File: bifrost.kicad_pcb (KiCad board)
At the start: 2 copper layers, 74 parts, among them J1 395430602, J10 Conn_0.1_01x04, J11 Conn_0.1_01x04, J12 Conn_0.1_01x06, J2 393800102, J3 393800102, J4 393800103, J5 393800103, J6 393800103, J7 393800103, J8 SJ_3524, J9 Conn_0.1_01x03, Q1 2N7002, SW1 SW_Push, SW2 SW_Push, SW3 SW_Push, SW4 SW_Push

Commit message: Begin placement
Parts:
- removed the C10 at (65.9, 49.0)
- removed the C12 at (89.1, 60.7)
- removed the C7 at (101.0, 19.0)
- removed the C8 at (50.8, 64.0)
- removed the C9 at (85.9, 34.0)
- removed the D5 at (68.1, 68.5)
- removed D6: BLU, LED_SMD:LED_1206_3216Metric_Pad1.42x1.75mm_HandSolder
- removed the J11 at (22.7, 62.8)
- removed the J3 at (51.6, 48.8)
- removed JP5, JP6: SolderJumper_2_Open, Jumper:SolderJumper-2_P1.3mm_Open_Pad1.0x1.5mm
- removed Q1: 2N7002, Package_TO_SOT_SMD:SOT-23
- removed the R13 at (113.1, 30.4)
- removed the R16 at (101.3, 38.2)
- removed the R17 at (78.2, 70.8)
- removed the R24 at (113.1, 33.4)
- removed the R25 at (83.0, 67.9)
- added C2: 0.1uF, Capacitor_SMD:C_0805_2012Metric_Pad1.15x1.40mm_HandSolder, F.Cu at (152.4, 35.6)
- added C3: 0.1uF, Capacitor_SMD:C_0805_2012Metric_Pad1.15x1.40mm_HandSolder, F.Cu at (137.9, 35.7)
- added C4: 0.1uF, Capacitor_SMD:C_0805_2012Metric_Pad1.15x1.40mm_HandSolder, F.Cu at (165.9, 21.2)
- added C5: 1uF, Capacitor_SMD:C_0805_2012Metric_Pad1.15x1.40mm_HandSolder, F.Cu at (158.2, 30.9)
- added C6: 0.1uF, Capacitor_SMD:C_0805_2012Metric_Pad1.15x1.40mm_HandSolder, F.Cu at (165.9, 24.1)
- added D1: RED, LED_SMD:LED_1206_3216Metric_Pad1.42x1.75mm_HandSolder, F.Cu at (132.5, 35.9)
- added J10: Conn_0.1_01x04, Connector_PinHeader_2.54mm:PinHeader_1x04_P2.54mm_Vertical, F.Cu at (22.7, 62.8)
- added J12: Micro_SD_Card_Det_Single, bifrost:microSD_Molex_1051620001, B.Cu at (179.6, 100.6)
- added R1: 1K, Resistor_SMD:R_0805_2012Metric_Pad1.15x1.40mm_HandSolder, F.Cu at (158.2, 33.9)
- added R14: 1K, Resistor_SMD:R_0805_2012Metric_Pad1.15x1.40mm_HandSolder, F.Cu at (163.0, 33.9)
- added R4: 2K, Resistor_SMD:R_0805_2012Metric_Pad1.15x1.40mm_HandSolder, F.Cu at (163.0, 30.9)
- added U1: 74LVC1G17, Package_TO_SOT_SMD:SOT-23-5_HandSoldering, F.Cu at (152.9, 31.8)
- added U2: 74LVC1G14, Package_TO_SOT_SMD:SOT-23-5_HandSoldering, F.Cu at (166.5, 17.4)
- added U3: 74AHCT125, Package_SO:SOIC-14_3.9x8.7mm_P1.27mm, F.Cu at (188.0, 104.1)
- D2: renamed from D4; value RED -> GRN
- D3: renamed from D2; value AMB -> BLU
- D4: renamed from D3; value AMB -> BLU
- D5: renamed from D1; value AMB -> BLU
- J1: value 395430602 -> 395430002
- J2: value 393800102 -> 395430002; footprint bifrost:TerminalBlock_Molex_393800102_1x02_P6.35mm_Horizontal -> bifrost:TerminalBlock_Molex_395430602_1x02_P5.00mm_Horizontal
- J3: renamed from J4; value 393800103 -> 393570003; footprint bifrost:TerminalBlock_Molex_393800103_1x03_P6.35mm_Horizontal -> bifrost:TerminalBlock_Molex_393570003_1x03_P3.50mm_Horizontal
- J4: renamed from J5; value 393800103 -> 393570003; footprint bifrost:TerminalBlock_Molex_393800103_1x03_P6.35mm_Horizontal -> bifrost:TerminalBlock_Molex_393570003_1x03_P3.50mm_Horizontal
- J5: renamed from J6; value 393800103 -> 393570003; footprint bifrost:TerminalBlock_Molex_393800103_1x03_P6.35mm_Horizontal -> bifrost:TerminalBlock_Molex_393570003_1x03_P3.50mm_Horizontal
- J6: renamed from J7; value 393800103 -> 393570003; footprint bifrost:TerminalBlock_Molex_393800103_1x03_P6.35mm_Horizontal -> bifrost:TerminalBlock_Molex_393570003_1x03_P3.50mm_Horizontal
- JP1, JP2: value Jumper_NC_Small -> Jumper_NO_Small
- JP3: value Jumper_NC_Dual -> Jumper_NO_Small; footprint Connector_PinHeader_2.54mm:PinHeader_1x03_P2.54mm_Vertical -> Connector_PinHeader_2.54mm:PinHeader_1x02_P2.54mm_Vertical
- JP4: value SolderJumper_2_Open -> Jumper_NO_Small; footprint Jumper:SolderJumper-2_P1.3mm_Open_Pad1.0x1.5mm -> Connector_PinHeader_2.54mm:PinHeader_1x02_P2.54mm_Vertical
- R15: renamed from R23; value 470 -> 330
- R16: renamed from R18; value 470 -> 330
- R17: renamed from R19; value 470 -> 330
- R18: renamed from R20; value 470 -> 330
- R9: value 100 -> 10K
- moved A1 215.6 mm to (218.4, 96.5), turned to 270 degrees
- moved H3 172.4 mm to (231.1, 134.6)
- moved J7 160.0 mm to (185.4, 121.9), turned to 90 degrees
- moved H2 141.5 mm to (231.0, 88.9)
- moved H4 129.0 mm to (185.4, 134.6)
- moved JP3 123.9 mm to (156.6, 24.6)
- moved H1 115.1 mm to (185.4, 88.9)
- moved R9 100.5 mm to (165.9, 27.1)
- moved J1 97.3 mm to (121.9, 40.6)
- moved JP1 84.0 mm to (161.2, 24.6)
- moved J2 60.6 mm to (142.2, 43.2)
- moved JP4 53.5 mm to (161.2, 17.4)
- moved JP2 45.5 mm to (156.6, 17.4)
- renumbered C11 to C1, C5 to C10, C4 to C11, C6 to C12, C1 to C7, C2 to C8, C3 to C9, J12 to J11, J8 to J7, J9 to J8, J10 to J9, R3 to R10, R4 to R12, R12 to R13, R5 to R19, R26 to R2, R14 to R20, R1 to R21, R7 to R22, R6 to R23, R15 to R24, R2 to R25, R8 to R26, R27 to R3, R28 to R5, R29 to R6, R21 to R7, R22 to R8, SW3 to SW2, SW2 to SW3
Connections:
- A1 pad 12: /LED1 -> /BTN4
- A1 pad 13: /LED2 -> /~CS
- A1 pad 14: /LED3 -> /MOSI
- A1 pad 15: /BTN4 -> /MISO
- A1 pad 16: Net-(A1-Pad16) -> /SCK
- A1 pad 22: Net-(A1-Pad22) -> /LED1
- A1 pad 25: Net-(A1-Pad25) -> /LED2
- A1 pad 26: Net-(A1-Pad26) -> /LED3
- A1 pad 27: Net-(A1-Pad27) -> /A5V
- A1 pad 29: Net-(A1-Pad29) -> GND
- D2 pad 1: GND -> Net-(D2-Pad1)
- D2 pad 2: Net-(D4-Pad2) -> +5V
- D3 pad 1: GND -> Net-(D3-Pad1)
- D3 pad 2: Net-(D2-Pad2) -> /LED1
- D4 pad 1: GND -> Net-(D4-Pad1)
- D4 pad 2: Net-(D3-Pad2) -> /LED2
- D5 pad 1: GND -> Net-(D5-Pad1)
- D5 pad 2: Net-(D1-Pad2) -> /LED3
- J2 pad 1: VCC -> +5V
- J3 pad 1: VCC -> +5V
- J4 pad 1: VCC -> +5V
- J5 pad 1: VDD -> +5V
- J6 pad 1: VDD -> +5V
- JP1 pad 1: +5V -> /A5V
- JP1 pad 2: Net-(A1-Pad27) -> +5V
- JP2 pad 1: Net-(A1-Pad29) -> Net-(JP2-Pad1)
- JP2 pad 2: GND -> Net-(A1-Pad2)
- JP3 pad 1: VCC -> Net-(A1-Pad28)
- JP3 pad 2: +5V -> /BT_RST
- JP4 pad 1: /BT_TX -> Net-(JP4-Pad1)
- JP4 pad 2: Net-(A1-Pad2) -> Net-(A1-Pad1)
- R15 pad 1: +5V -> Net-(D2-Pad1)
- R15 pad 2: Net-(D4-Pad2) -> GND
- R16 pad 1: /LED1 -> Net-(D3-Pad1)
- R16 pad 2: Net-(D1-Pad2) -> GND
- R17 pad 1: /LED2 -> Net-(D4-Pad1)
- R17 pad 2: Net-(D2-Pad2) -> GND
- R18 pad 1: /LED3 -> Net-(D5-Pad1)
- R18 pad 2: Net-(D3-Pad2) -> GND
- R9 pad 1: Net-(Q1-Pad1) -> /BT_ST
- R9 pad 2: /BT_ST -> GND

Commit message: Do most placement
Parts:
- removed the JP3 at (156.6, 24.6)
- removed the R2 at (103.3, 44.1)
- added JP2: Jumper_NO_Small, Connector_PinHeader_2.54mm:PinHeader_1x02_P2.54mm_Vertical, F.Cu at (162.6, 80.0)
- added R4: 330, Resistor_SMD:R_0805_2012Metric_Pad1.15x1.40mm_HandSolder, B.Cu at (170.2, 62.2)
- A1: footprint bifrost:Arduino_Nano -> Module:Arduino_Nano
- C1, C10, C11, C12, C2, C3, C4, C5, C6, C7, C8, C9, R1, R10, R11, R12, R13, R14, R15, R16, R17, R18, R19, R20, R21, R22, R23, R24, R25, R26, R3, R5, R6, R7, R8, R9: moved to B.Cu
- J11: footprint Connector_PinSocket_2.54mm:PinSocket_1x08_P2.54mm_Vertical -> Connector_PinSocket_2.54mm:PinSocket_1x06_P2.54mm_Vertical
- R2: renamed from R4; moved to B.Cu
- moved J9 182.6 mm to (199.1, 86.4)
- moved J10 180.1 mm to (199.1, 99.1)
- moved J11 174.1 mm to (199.1, 80.0), turned to 180 degrees
- moved J3 147.7 mm to (186.7, 56.9), turned to 180 degrees
- moved C12 138.5 mm to (187.3, 106.7), turned to 90 degrees
- moved C9 136.9 mm to (179.1, 113.0), turned to 90 degrees
- moved R25 126.4 mm to (185.4, 119.4), turned to 90 degrees
- moved SW1 122.1 mm to (172.4, 110.6), turned to 45 degrees
- moved SW3 121.3 mm to (179.3, 117.4), turned to 45 degrees
- moved SW4 121.2 mm to (186.0, 110.6), turned to 45 degrees
- moved J4 115.1 mm to (174.0, 56.9), turned to 180 degrees
- moved R26 115.0 mm to (190.5, 109.9), turned to 90 degrees
- moved D5 111.8 mm to (162.6, 111.8), turned to 90 degrees
- moved SW2 110.9 mm to (179.2, 103.8), turned to 45 degrees
- moved R22 110.5 mm to (181.0, 100.3), turned to 90 degrees
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- renumbered JP2 to JP3
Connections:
- J1 pad 1: VBUS -> GND
- J1 pad 2: GND -> VBUS
- R3 pad 1: Net-(A1-Pad9) -> Net-(A1-Pad8)
- R3 pad 2: /OUT2 -> /OUT1
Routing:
- added copper zone on B.Cu, net GND
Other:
- board outline added: 73.7 x 71.1 mm

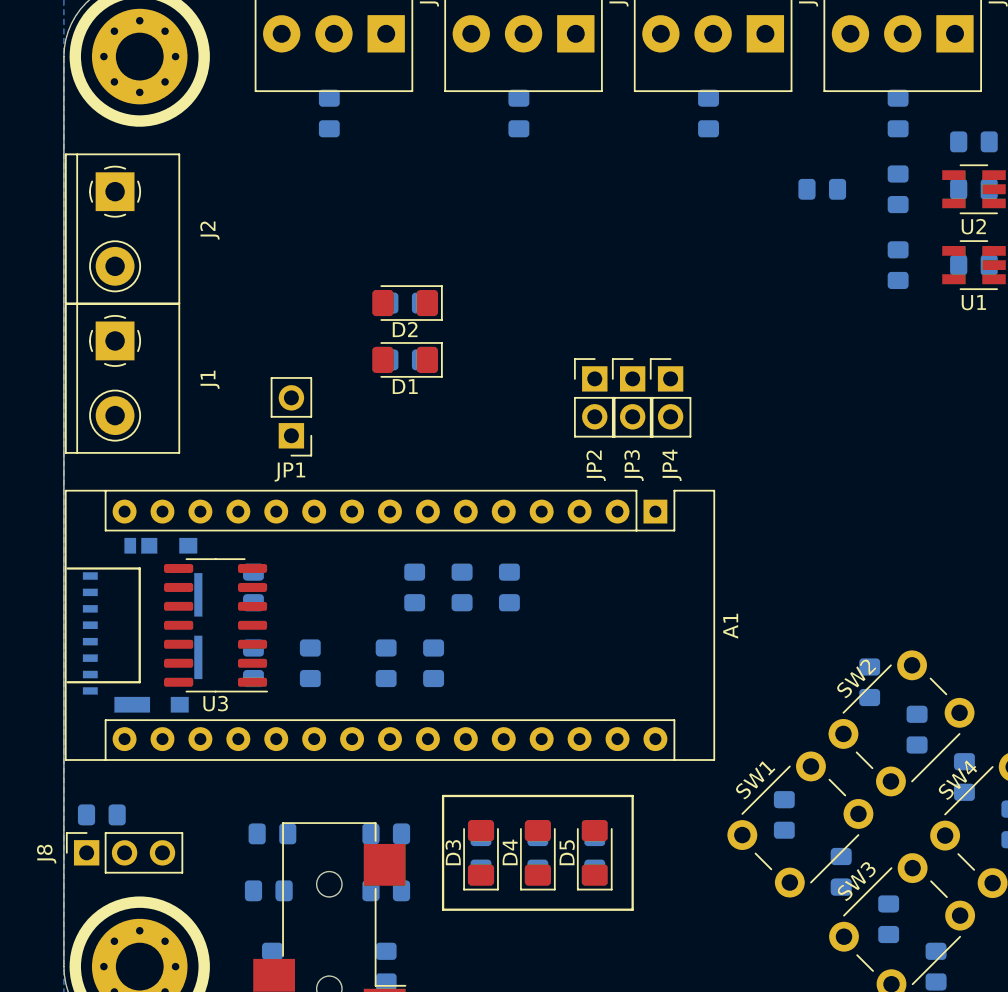
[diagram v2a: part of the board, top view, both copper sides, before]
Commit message: Move some footprints and designators around
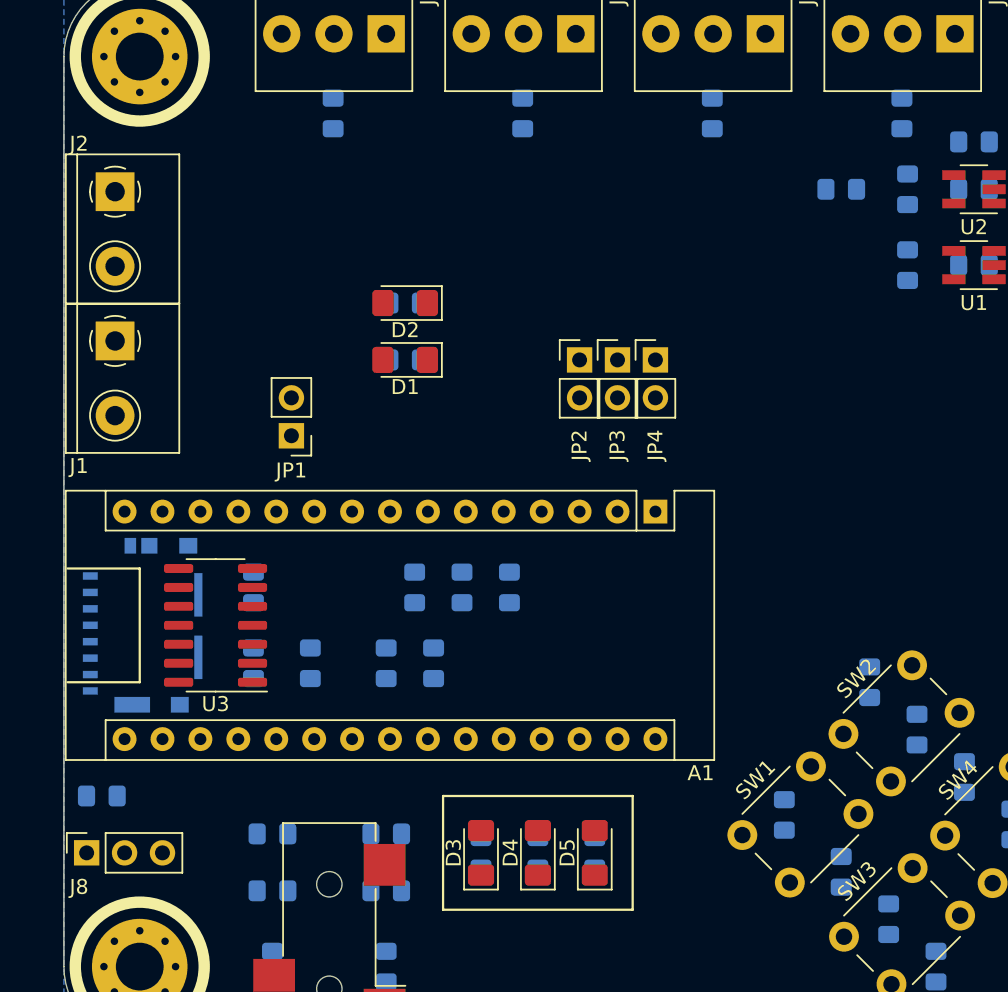
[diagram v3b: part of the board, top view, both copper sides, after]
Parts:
- moved JP2 1.63 mm to (161.5, 78.7)
- moved JP3 1.63 mm to (164.1, 78.7)
- moved JP4 1.63 mm to (166.6, 78.7)
- moved C1 1.27 mm to (129.5, 108.0)
- moved C3 1.27 mm to (179.1, 67.3)
- moved R1 0.63 mm to (183.5, 72.4)
- moved R2 0.63 mm to (183.5, 67.3)
- moved R5 0.25 mm to (157.7, 62.2)
- moved R3 0.25 mm to (183.1, 62.2)
- moved R4 0.25 mm to (170.4, 62.2)
- moved R6 0.25 mm to (145.0, 62.2)
- moved R13 0.25 mm to (141.0, 114.3)
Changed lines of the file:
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@@
     (descr "Arduino Nano, http://www.mouser.com/pdfdocs/Gravitech_Arduino_Nano3_0.pdf")
     (tags "Arduino Nano")
-    (fp_text reference A1 (at 7.62 -5.08 90) (layer F.SilkS)
+    (fp_text reference A1 (at 17.526 -3.048 180) (layer F.SilkS)
       (effects (font (size 1 1) (thickness 0.15)))
     )
@@
   )
   (module Resistor_SMD:R_0805_2012Metric_Pad1.15x1.40mm_HandSolder (layer B.Cu)
-    (at 182.88 67.31 90)
+    (at 183.515 67.31 90)
     (descr "Resistor SMD 0805 (2012 Metric), square (rectangular) end terminal, IPC_7351 nominal with elongated pad for handsoldering. (Body size source: https://docs.google.com/spreadsheets/d/1BsfQQcO9C6DZCsRaXUlFlo91Tg2WpOkGARC1WS5S8t0/edit?usp=sharing), generated with kicad-footprint-generator")
     (tags "resistor handsolder")
@@
   )
   (module Resistor_SMD:R_0805_2012Metric_Pad1.15x1.40mm_HandSolder (layer B.Cu)
-    (at 182.88 72.39 90)
+    (at 183.515 72.39 90)
     (descr "Resistor SMD 0805 (2012 Metric), square (rectangular) end terminal, IPC_7351 nominal with elongated pad for handsoldering. (Body size source: https://docs.google.com/spreadsheets/d/1BsfQQcO9C6DZCsRaXUlFlo91Tg2WpOkGARC1WS5S8t0/edit?usp=sharing), generated with kicad-footprint-generator")
     (tags "resistor handsolder")
@@
   )
   (module Connector_PinHeader_2.54mm:PinHeader_1x02_P2.54mm_Vertical (layer F.Cu)
-    (at 167.64 80.01)
+    (at 166.624 78.74)
     (descr "Through hole straight pin header, 1x02, 2.54mm pitch, single row")
     (tags "Through hole pin header THT 1x02 2.54mm single row")
@@
   )
   (module Connector_PinHeader_2.54mm:PinHeader_1x02_P2.54mm_Vertical (layer F.Cu)
-    (at 162.56 80.01)
+    (at 161.544 78.74)
     (descr "Through hole straight pin header, 1x02, 2.54mm pitch, single row")
     (tags "Through hole pin header THT 1x02 2.54mm single row")
@@
   )
   (module Connector_PinHeader_2.54mm:PinHeader_1x02_P2.54mm_Vertical (layer F.Cu)
-    (at 165.1 80.01)
+    (at 164.084 78.74)
     (descr "Through hole straight pin header, 1x02, 2.54mm pitch, single row")
     (tags "Through hole pin header THT 1x02 2.54mm single row")
@@
     (descr "Terminal Block Phoenix MKDS-1,5-2, 2 pins, pitch 5mm, size 10x9.8mm^2, drill diamater 1.3mm, pad diameter 2.6mm, see http://www.farnell.com/datasheets/100425.pdf, script-generated using https://github.com/pointhi/kicad-footprint-generator/scripts/TerminalBlock_Phoenix")
     (tags "THT Terminal Block Phoenix MKDS-1,5-2 pitch 5mm size 10x9.8mm^2 drill 1.3mm pad 2.6mm")
-    (fp_text reference J2 (at 2.5 -6.26 90) (layer F.SilkS)
+    (fp_text reference J2 (at -3.208 2.413 180) (layer F.SilkS)
       (effects (font (size 1 1) (thickness 0.15)))
     )
@@
     (descr "Terminal Block Phoenix MKDS-1,5-2, 2 pins, pitch 5mm, size 10x9.8mm^2, drill diamater 1.3mm, pad diameter 2.6mm, see http://www.farnell.com/datasheets/100425.pdf, script-generated using https://github.com/pointhi/kicad-footprint-generator/scripts/TerminalBlock_Phoenix")
     (tags "THT Terminal Block Phoenix MKDS-1,5-2 pitch 5mm size 10x9.8mm^2 drill 1.3mm pad 2.6mm")
-    (fp_text reference J1 (at 2.5 -6.26 90) (layer F.SilkS)
+    (fp_text reference J1 (at 8.382 2.413 180) (layer F.SilkS)
       (effects (font (size 1 1) (thickness 0.15)))
     )
@@
   )
   (module Capacitor_SMD:C_0805_2012Metric_Pad1.15x1.40mm_HandSolder (layer B.Cu)
-    (at 177.8 67.31)
+    (at 179.07 67.31)
     (descr "Capacitor SMD 0805 (2012 Metric), square (rectangular) end terminal, IPC_7351 nominal with elongated pad for handsoldering. (Body size source: https://docs.google.com/spreadsheets/d/1BsfQQcO9C6DZCsRaXUlFlo91Tg2WpOkGARC1WS5S8t0/edit?usp=sharing), generated with kicad-footprint-generator")
     (tags "capacitor handsolder")
@@
   )
   (module Resistor_SMD:R_0805_2012Metric_Pad1.15x1.40mm_HandSolder (layer B.Cu)
-    (at 144.78 62.23 90)
+    (at 145.034 62.23 90)
     (descr "Resistor SMD 0805 (2012 Metric), square (rectangular) end terminal, IPC_7351 nominal with elongated pad for handsoldering. (Body size source: https://docs.google.com/spreadsheets/d/1BsfQQcO9C6DZCsRaXUlFlo91Tg2WpOkGARC1WS5S8t0/edit?usp=sharing), generated with kicad-footprint-generator")
     (tags "resistor handsolder")
@@
   )
   (module Resistor_SMD:R_0805_2012Metric_Pad1.15x1.40mm_HandSolder (layer B.Cu)
-    (at 157.48 62.23 90)
+    (at 157.734 62.23 90)
     (descr "Resistor SMD 0805 (2012 Metric), square (rectangular) end terminal, IPC_7351 nominal with elongated pad for handsoldering. (Body size source: https://docs.google.com/spreadsheets/d/1BsfQQcO9C6DZCsRaXUlFlo91Tg2WpOkGARC1WS5S8t0/edit?usp=sharing), generated with kicad-footprint-generator")
     (tags "resistor handsolder")
@@
   )
   (module Resistor_SMD:R_0805_2012Metric_Pad1.15x1.40mm_HandSolder (layer B.Cu)
-    (at 170.18 62.23 90)
+    (at 170.434 62.23 90)
     (descr "Resistor SMD 0805 (2012 Metric), square (rectangular) end terminal, IPC_7351 nominal with elongated pad for handsoldering. (Body size source: https://docs.google.com/spreadsheets/d/1BsfQQcO9C6DZCsRaXUlFlo91Tg2WpOkGARC1WS5S8t0/edit?usp=sharing), generated with kicad-footprint-generator")
     (tags "resistor handsolder")
@@
   )
   (module Resistor_SMD:R_0805_2012Metric_Pad1.15x1.40mm_HandSolder (layer B.Cu)
-    (at 182.88 62.23 90)
+    (at 183.134 62.23 90)
     (descr "Resistor SMD 0805 (2012 Metric), square (rectangular) end terminal, IPC_7351 nominal with elongated pad for handsoldering. (Body size source: https://docs.google.com/spreadsheets/d/1BsfQQcO9C6DZCsRaXUlFlo91Tg2WpOkGARC1WS5S8t0/edit?usp=sharing), generated with kicad-footprint-generator")
     (tags "resistor handsolder")
@@
   )
   (module Resistor_SMD:R_0805_2012Metric_Pad1.15x1.40mm_HandSolder (layer B.Cu)
-    (at 140.725 114.3)
+    (at 140.97 114.3)
     (descr "Resistor SMD 0805 (2012 Metric), square (rectangular) end terminal, IPC_7351 nominal with elongated pad for handsoldering. (Body size source: https://docs.google.com/spreadsheets/d/1BsfQQcO9C6DZCsRaXUlFlo91Tg2WpOkGARC1WS5S8t0/edit?usp=sharing), generated with kicad-footprint-generator")
     (tags "resistor handsolder")
@@
     (descr "Through hole straight socket strip, 1x03, 2.54mm pitch, single row (from Kicad 4.0.7), script generated")
     (tags "Through hole socket strip THT 1x03 2.54mm single row")
-    (fp_text reference J8 (at 0 -2.77 90) (layer F.SilkS)
+    (fp_text reference J8 (at -2.286 -0.508 180) (layer F.SilkS)
       (effects (font (size 1 1) (thickness 0.15)))
     )
@@
   )
   (module Capacitor_SMD:C_0805_2012Metric_Pad1.15x1.40mm_HandSolder (layer B.Cu)
-    (at 129.54 109.22)
+    (at 129.54 107.95)
     (descr "Capacitor SMD 0805 (2012 Metric), square (rectangular) end terminal, IPC_7351 nominal with elongated pad for handsoldering. (Body size source: https://docs.google.com/spreadsheets/d/1BsfQQcO9C6DZCsRaXUlFlo91Tg2WpOkGARC1WS5S8t0/edit?usp=sharing), generated with kicad-footprint-generator")
     (tags "capacitor handsolder")
